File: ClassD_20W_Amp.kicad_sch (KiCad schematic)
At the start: 14 parts, among them U2 PAM8320RDR

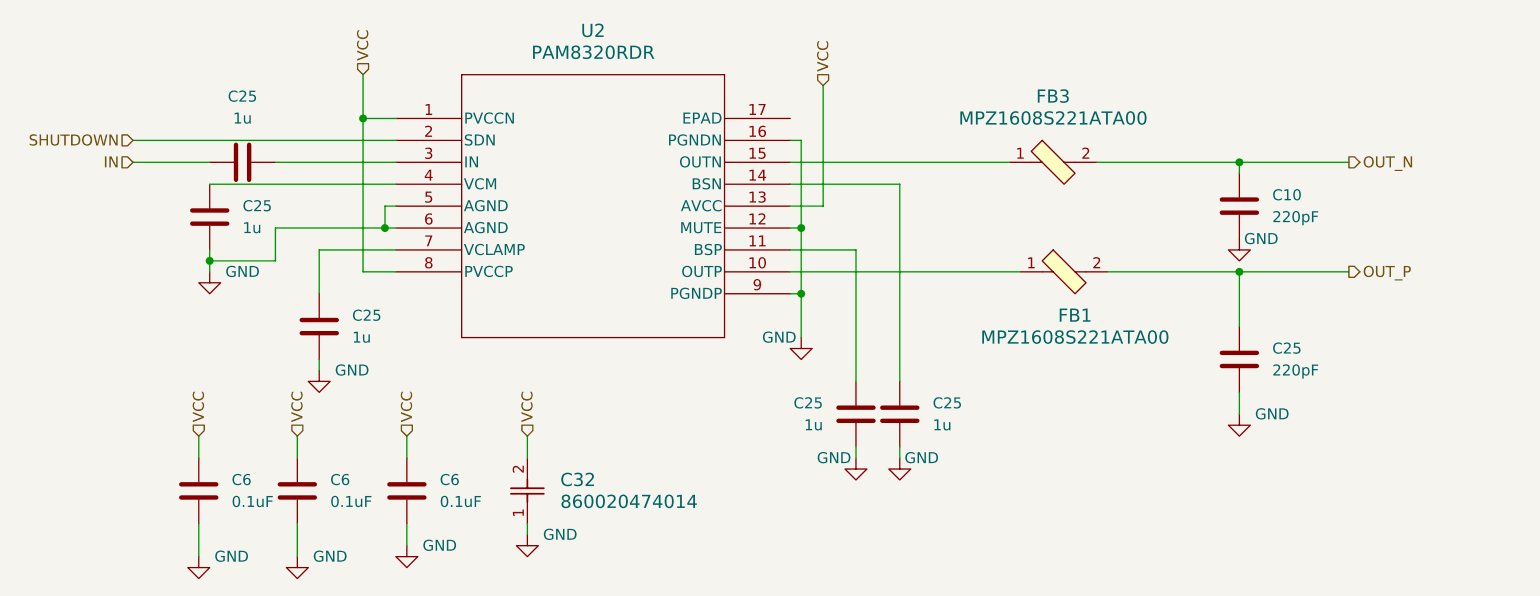
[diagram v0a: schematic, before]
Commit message: add usb host current limit and ESD diodes
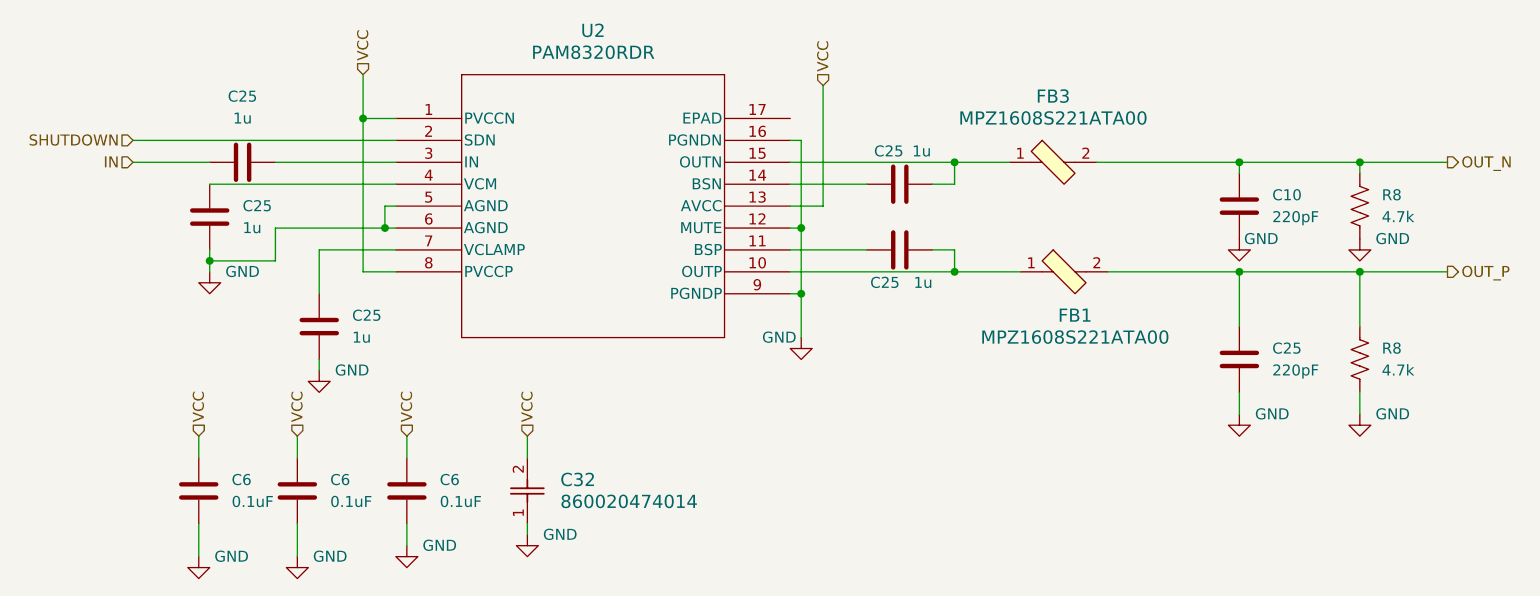
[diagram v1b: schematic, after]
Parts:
- added R8 (x2): 4.7k, Resistor_SMD:R_0402_1005Metric, symbol Device:R_US
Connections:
- net GND: now also R8.2, R8.2; no longer C25.2, C25.2
- net OUT_N: now also R8.1
- net OUT_P: now also R8.1
- net at FB1.1, U2.10 (OUTP): now also C25.2
- net at FB3.1, U2.15 (OUTN): now also C25.2
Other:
- moved on the sheet: C25

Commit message: getting closer
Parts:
- added R8: 0, Resistor_SMD:R_0402_1005Metric, symbol Device:R_US
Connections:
- net at U2.3 (IN): now also R8.2; no longer C25.2
- new net: C25.2, R8.1
- no-connect marks 0 -> 1
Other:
- moved on the sheet: C25
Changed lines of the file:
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@@
   (junction (at 149.86 90.17) (diameter 0) (color 0 0 0 0)
   )
+  (no_connect (at 130.81 72.39))
   (wire (pts (xy 86.36 121.92) (xy 86.36 119.38))
     (stroke (width 0) (type default))
@@
     (stroke (width 0) (type default))
   )
+  (wire (pts (xy 74.93 77.47) (xy 85.09 77.47))
+    (stroke (width 0) (type default))
+  )
   (wire (pts (xy 147.32 87.63) (xy 149.86 87.63))
     (stroke (width 0) (type default))
@@
     (stroke (width 0) (type default))
   )
-  (wire (pts (xy 71.12 77.47) (xy 85.09 77.47))
-    (stroke (width 0) (type default))
-  )
-  (wire (pts (xy 54.61 77.47) (xy 63.5 77.47))
+  (wire (pts (xy 66.04 77.47) (xy 67.31 77.47))
+    (stroke (width 0) (type default))
+  )
+  (wire (pts (xy 54.61 77.47) (xy 58.42 77.47))
     (stroke (width 0) (type default))
   )
@@
     )
   )
-  (symbol (lib_id "Device:C") (at 67.31 77.47 90) (unit 1)
-    (in_bom yes) (on_board yes) (dnp no) (fields_autoplaced)
-    (property "Reference" "C25" (at 67.31 69.85 90)
-      (effects (font (size 1.27 1.27)))
-    )
-    (property "Value" "1u" (at 67.31 72.39 90)
-      (effects (font (size 1.27 1.27)))
-    )
-    (property "Footprint" "Capacitor_SMD:C_0603_1608Metric" (at 71.12 76.5048 0)
-      (effects (font (size 1.27 1.27)) hide)
-    )
-    (property "Datasheet" "~" (at 67.31 77.47 0)
+  (symbol (lib_id "Device:C") (at 62.23 77.47 90) (unit 1)
+    (in_bom yes) (on_board yes) (dnp no) (fields_autoplaced)
+    (property "Reference" "C25" (at 62.23 69.85 90)
+      (effects (font (size 1.27 1.27)))
+    )
+    (property "Value" "1u" (at 62.23 72.39 90)
+      (effects (font (size 1.27 1.27)))
+    )
+    (property "Footprint" "Capacitor_SMD:C_0603_1608Metric" (at 66.04 76.5048 0)
+      (effects (font (size 1.27 1.27)) hide)
+    )
+    (property "Datasheet" "~" (at 62.23 77.47 0)
       (effects (font (size 1.27 1.27)) hide)
     )
@@
         )
       )
+    )
+  )
+  (symbol (lib_id "Device:R_US") (at 71.12 77.47 90) (unit 1)
+    (in_bom yes) (on_board yes) (dnp no) (fields_autoplaced)
+    (property "Reference" "R8" (at 71.12 71.12 90)
+      (effects (font (size 1.27 1.27)))
+    )
+    (property "Value" "0" (at 71.12 73.66 90)
+      (effects (font (size 1.27 1.27)))
+    )
+    (property "Footprint" "Resistor_SMD:R_0402_1005Metric" (at 71.374 76.454 90)
+      (effects (font (size 1.27 1.27)) hide)
+    )
+    (property "Datasheet" "~" (at 71.12 77.47 0)
+      (effects (font (size 1.27 1.27)) hide)
+    )
+    (pin "1")
+    (pin "2")
+    (instances
+      (project "DaisySeedBreakout"
+        (path "/a83c9f4b-f61b-47d4-b39d-4636bff6eb0e"
+          (reference "R8") (unit 1)
+        )
+        (path "/a83c9f4b-f61b-47d4-b39d-4636bff6eb0e/a0f8a1fd-6189-4b02-8cf7-e8d7538f4e50"
+          (reference "R23") (unit 1)
+        )
+        (path "/a83c9f4b-f61b-47d4-b39d-4636bff6eb0e/b269dd26-915f-458b-a2d7-e1fbc9f1daa5"
+          (reference "R65") (unit 1)
+        )
+      )
